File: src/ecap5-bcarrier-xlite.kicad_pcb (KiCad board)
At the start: 4 copper layers, 161.3 x 55.2 mm, 55 parts, among them J1 DDR4_SODIMM_Board, J2 DDR4_SODIMM_Board, J3 Conn_01x04, J4 Conn_01x04, J5 USB_C_Receptacle_USB2.0_14P, J6 Conn_Coaxial, J7 Conn_Coaxial, J8 Conn_Coaxial, J9 1935161, Q1 BC846BR13, Q2 BC846BR13, SW1 RESET_SOM1, SW2 RESET_SOM2, SW3 USER1, SW4 USER1, U1 FT232RN, U2 AP7375-33SA-7

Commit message: Save button footprint in local library
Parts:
- SW1, SW2, SW3, SW4: footprint Button_Switch_SMD:SW_Push_1P1T_NO_CK_PTS125Sx73SMTR -> ECAP5-BCARRIER-XLITE:SW_Push_1P1T_NO_CK_PTS125Sx73SMTR_1

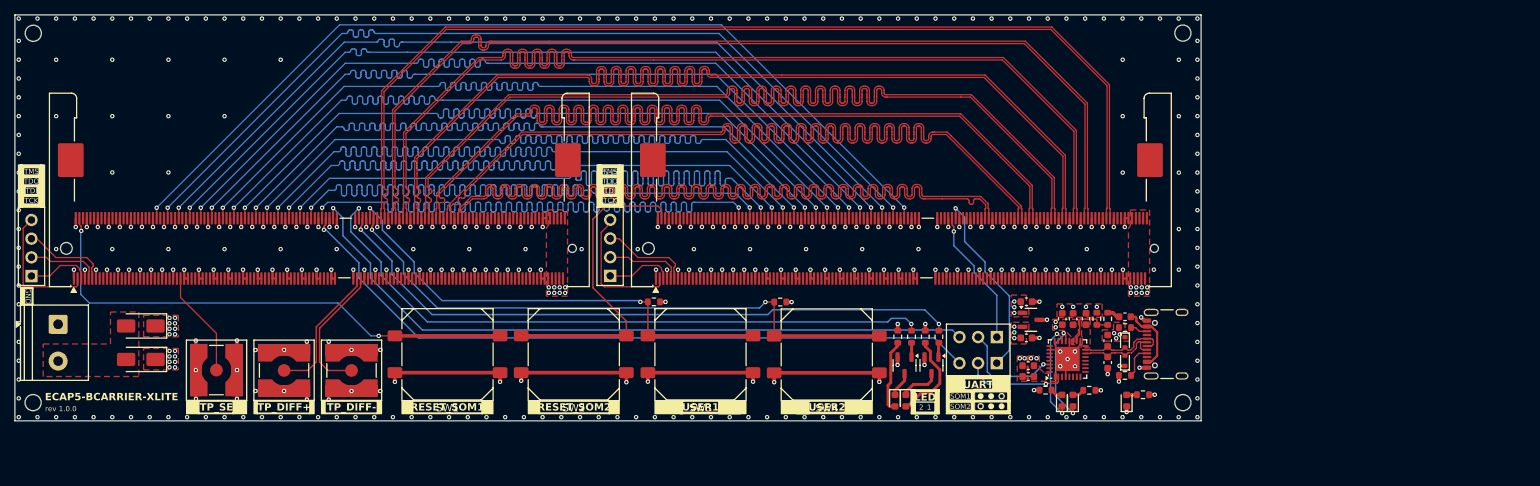
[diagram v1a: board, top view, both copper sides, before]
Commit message: Fix some drc errors
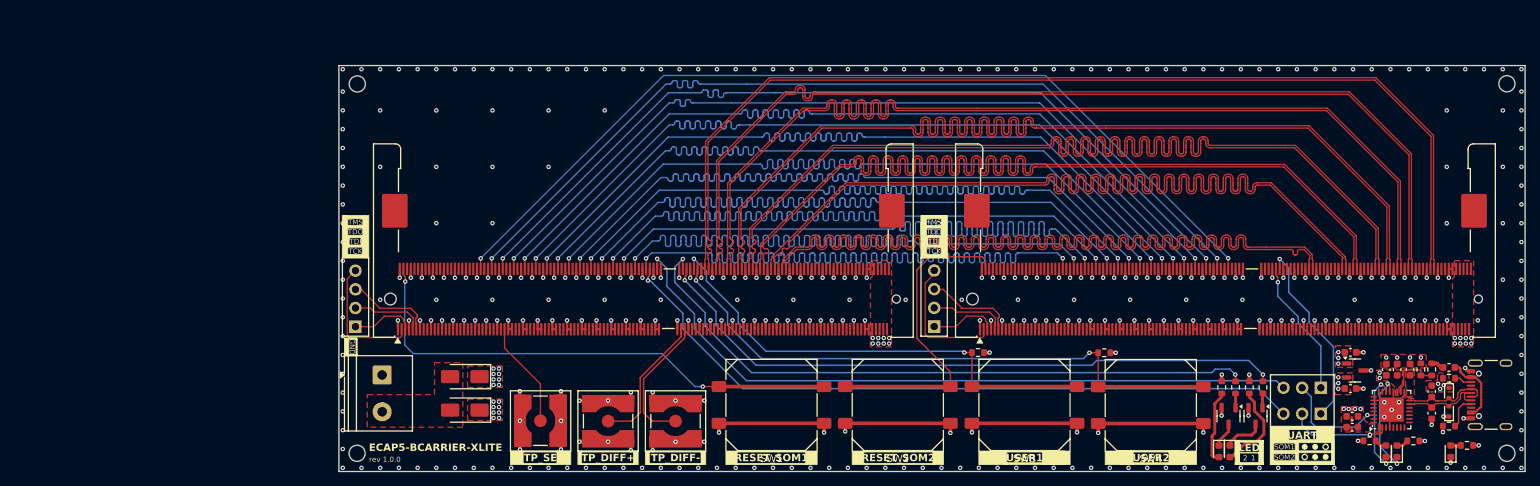
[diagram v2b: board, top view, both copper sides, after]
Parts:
- moved SW3 44.6 mm to (168.2, 116.0)
- moved J6 44.6 mm to (102.4, 118.2)
- moved C1 44.6 mm to (212.6, 108.9)
- moved C2 44.6 mm to (212.6, 113.8)
- moved C3 44.6 mm to (217.4, 111.2)
- moved C4 44.6 mm to (218.9, 111.2)
- moved C5 44.6 mm to (212.8, 117.6)
- moved C6 44.6 mm to (212.8, 119.1)
- moved C7 44.6 mm to (223.6, 117.2)
- moved C8 44.6 mm to (223.6, 114.2)
- moved C9 44.6 mm to (220.7, 111.2)
- moved D1 44.6 mm to (92.1, 116.7)
- moved D2 44.6 mm to (194.7, 122.3)
- moved D3 44.6 mm to (226.0, 116.9)
- moved D4 44.6 mm to (226.0, 114.4)
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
